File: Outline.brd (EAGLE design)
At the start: 53.8 x 53.8 mm, 51 parts, among them CN1 0675031020, IC1 ATXMEGA32A4U-AU, IC2 ST1480ACDR, J1 RJHSE5080, J2 J2, U1 NCP1117DTAG @ 3.3v, U2 NCP1117DTAG @ 12v

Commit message: 4.2.4
Final Version Submitted aka v1.0
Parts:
- moved C15 0.51 mm to (44.2, 19.8)
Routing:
- net +12V: track 85.4 -> 86.2 mm
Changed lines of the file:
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@@
 </element>
 <element name="C7" library="SparkFun" package="0603-CAP" value=".1uF" x="47.4321" y="40.4558125" smashed="yes">
-<attribute name="NAME" x="49.110178125" y="40.065784375" size="0.8128" layer="25"/>
+<attribute name="NAME" x="46.697178125" y="41.335784375" size="0.8128" layer="25"/>
 </element>
 <element name="DRV0" library="1dah" package="SOT89-5" value="PT4115" x="7.112" y="34.544">
@@
 </element>
 <element name="R8" library="nonolith" package="0805" value="300m Ohm" x="3.81" y="8.382" smashed="yes" rot="R180">
-<attribute name="NAME" x="5.842" y="7.493" size="0.8128" layer="25" font="vector" ratio="10"/>
+<attribute name="NAME" x="0.254" y="7.239" size="0.8128" layer="25" font="vector" ratio="10"/>
 </element>
 <element name="DRV2" library="1dah" package="SOT89-5" value="PT4115" x="12.446" y="12.446" rot="R180">
@@
 </element>
 <element name="R9" library="nonolith" package="0805" value="300 mOhm" x="12.192" y="8.382" smashed="yes" rot="R180">
-<attribute name="NAME" x="14.224" y="7.493" size="0.8128" layer="25" font="vector" ratio="10"/>
+<attribute name="NAME" x="8.636" y="7.239" size="0.8128" layer="25" font="vector" ratio="10"/>
 </element>
 <element name="J1" library="TechIsCool" package="RJHSE5080" value="RJHSE5080" x="19.304" y="-1.016" smashed="yes">
@@
 </element>
 <element name="R10" library="nonolith" package="0603" value="10k Ohm" x="50.8" y="40.38599375" smashed="yes">
-<attribute name="NAME" x="49.149" y="40.76700625" size="0.8128" layer="25" ratio="10" rot="R180"/>
+<attribute name="NAME" x="52.70499375" y="41.402" size="0.8128" layer="25" ratio="10" rot="R270"/>
 </element>
 <element name="R11" library="nonolith" package="0603" value="1k Ohm" x="50.79999375" y="42.545" smashed="yes">
-<attribute name="NAME" x="46.98999375" y="42.164" size="0.8128" layer="25" ratio="10"/>
+<attribute name="NAME" x="49.78399375" y="43.434" size="0.8128" layer="25" ratio="10"/>
 </element>
 <element name="R12" library="nonolith" package="0603" value="10k Ohm" x="46.30728125" y="50.950375" smashed="yes" rot="R90">
@@
 </element>
 <element name="R15" library="nonolith" package="0603" value="10k" x="40.1828" y="32.766" smashed="yes" rot="R270">
-<attribute name="NAME" x="40.5638" y="34.417" size="0.762" layer="25" ratio="10" rot="R90"/>
+<attribute name="NAME" x="40.259" y="35.2298" size="0.762" layer="25" ratio="10" rot="R180"/>
 </element>
 <element name="C9" library="SparkFun" package="0603-CAP" value=".1uF" x="2.286" y="43.942" smashed="yes" rot="R270">
@@
 <attribute name="NAME" x="51.816" y="10.668" size="0.8128" layer="25" rot="R180"/>
 </element>
-<element name="C15" library="SparkFun" package="0603-CAP" value=".1uF" x="44.196" y="19.304" smashed="yes" rot="R180">
-<attribute name="NAME" x="42.545" y="19.685" size="0.8128" layer="25" rot="R180"/>
+<element name="C15" library="SparkFun" package="0603-CAP" value=".1uF" x="44.196" y="19.812" smashed="yes" rot="R180">
+<attribute name="NAME" x="42.545" y="20.193" size="0.8128" layer="25" rot="R180"/>
 </element>
 <element name="U$1" library="TechIsCool" package="DMG1012T" value="DMG1012T" x="49.784" y="7.366" smashed="yes" rot="R180"/>
@@
 </element>
 <element name="U$3" library="TechIsCool" package="10W_LED" value="10W_RGB_LED" x="27.0256" y="26.5684" smashed="yes">
-<attribute name="NAME" x="36.3336" y="32.3494" size="1.27" layer="25" font="vector"/>
 <attribute name="VALUE" x="20.5856" y="26.9534" size="1.27" layer="27" font="vector"/>
 </element>
@@
 <contactref element="CN1" pad="GND@4"/>
 <contactref element="R15" pad="2"/>
-<via x="15.113" y="32.004" extent="1-16" drill="0.6" diameter="0.8128"/>
+<via x="13.716" y="32.004" extent="1-16" drill="0.6" diameter="0.8128"/>
 <via x="12.446" y="49.022" extent="1-16" drill="0.6" diameter="0.8128"/>
 <via x="5.461" y="12.192" extent="1-16" drill="0.6" diameter="0.8128"/>
@@
 <wire x1="48.2574" y1="38.0974" x2="46.3148" y2="38.0974" width="0.4064" layer="1"/>
 <wire x1="38.354" y1="33.186" x2="38.354" y2="33.274" width="0.4064" layer="1"/>
-<via x="40.513" y="35.433" extent="1-16" drill="0.6" diameter="0.8128"/>
+<via x="41.021" y="35.433" extent="1-16" drill="0.6" diameter="0.8128"/>
 <wire x1="19.47084375" y1="41.695840625" x2="19.812" y2="42.036996875" width="0.4064" layer="1"/>
 <wire x1="19.47084375" y1="41.695840625" x2="19.939003125" y2="42.164" width="0.4064" layer="16"/>
@@
 <wire x1="42.9182" y1="14.7946" x2="44.7816" y2="16.658" width="0.8128" layer="1"/>
 <wire x1="44.7816" y1="16.658" x2="45.046" y2="16.9224" width="0.8128" layer="1"/>
-<wire x1="45.046" y1="16.9224" x2="45.046" y2="19.304" width="0.8128" layer="1"/>
-<wire x1="45.046" y1="19.304" x2="47.2968" y2="21.5548" width="0.8128" layer="1"/>
-<wire x1="47.2968" y1="21.5548" x2="48.0412" y2="21.5548" width="0.8128" layer="1"/>
+<wire x1="45.046" y1="16.9224" x2="45.046" y2="19.812" width="0.8128" layer="1"/>
+<wire x1="47.2968" y1="21.5548" x2="47.752" y2="21.5548" width="0.8128" layer="1"/>
+<wire x1="47.752" y1="21.5548" x2="48.0412" y2="21.5548" width="0.8128" layer="1"/>
 <wire x1="41.148" y1="12.7" x2="42.125" y2="13.677" width="0.8128" layer="1"/>
 <wire x1="42.125" y1="13.677" x2="42.926" y2="13.677" width="0.8128" layer="1"/>
@@
 <wire x1="11.684" y1="17.78" x2="11.684" y2="34.036" width="0.8128" layer="16"/>
 <wire x1="11.684" y1="34.036" x2="11.176" y2="34.544" width="0.8128" layer="16"/>
+<wire x1="45.046" y1="19.812" x2="46.0092" y2="19.812" width="0.8128" layer="1"/>
+<wire x1="46.0092" y1="19.812" x2="47.752" y2="21.5548" width="0.8128" layer="1"/>
 </signal>
 <signal name="N$2">

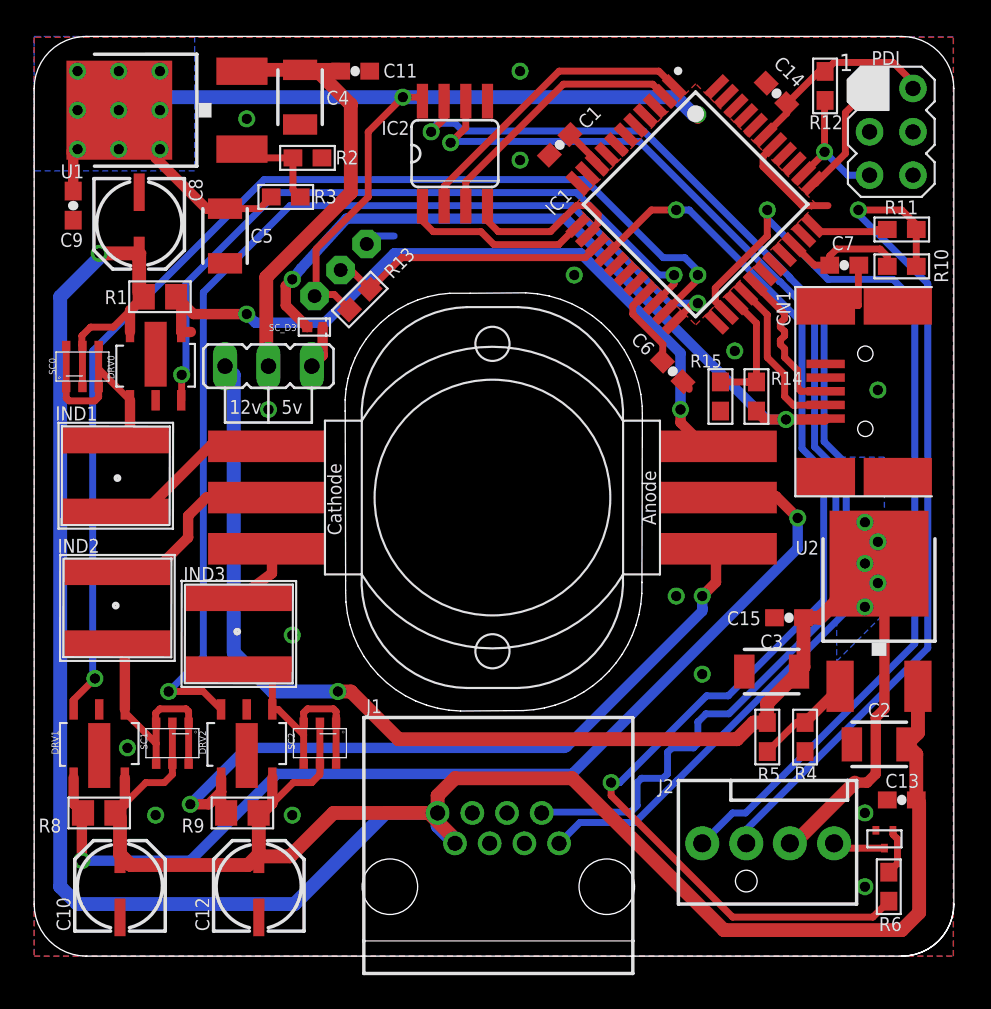
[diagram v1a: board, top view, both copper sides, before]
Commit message: 4.3
Changed LDO resistor values to stop overheating. Added 68pf cap between
reset and ground to make AVR Dragon talk with device.
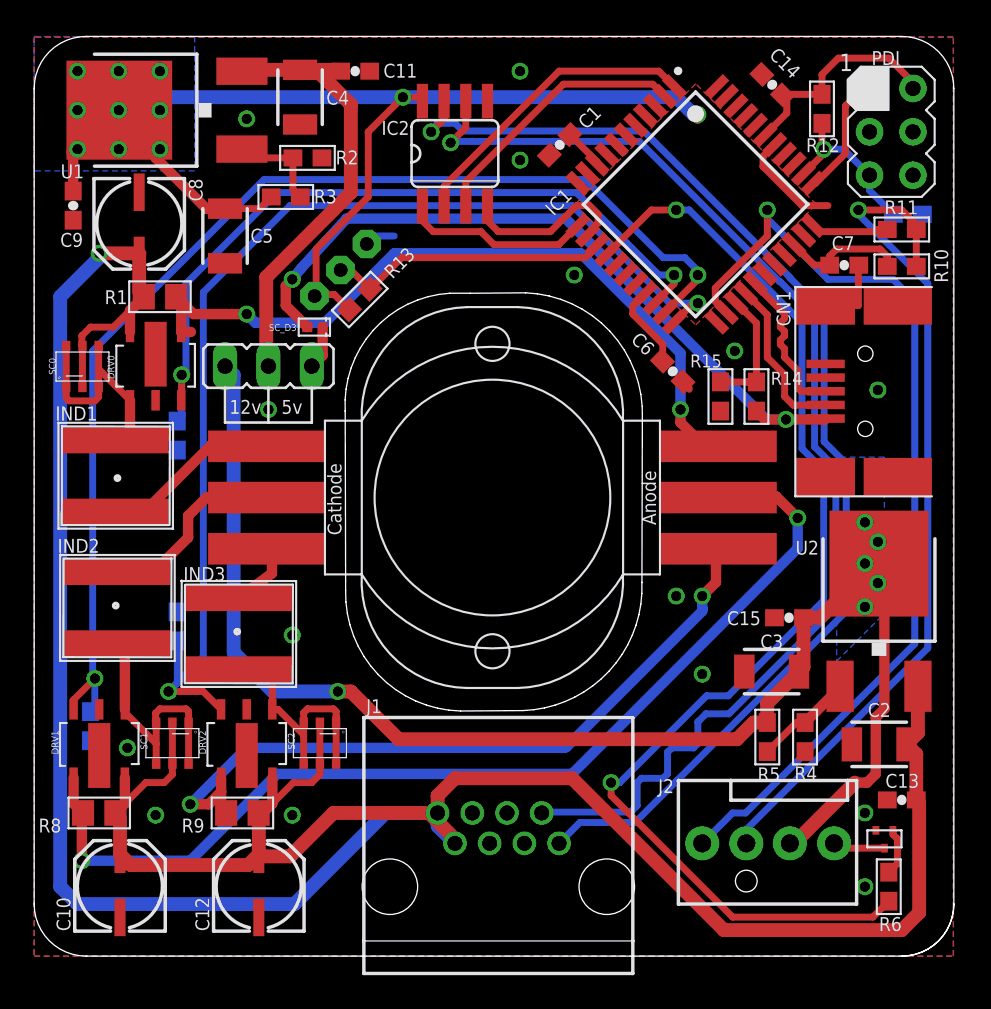
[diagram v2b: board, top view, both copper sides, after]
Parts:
- added C16: 68pF, SparkFun:0603-CAP
- added R16, R17, R7: 47k Ohm, nonolith:0603
- R2: value 15 Ohms -> 412 Ohms
- R3: value 9.09 Ohms -> 255 Ohms
- R4: value 102 Ohms -> 2k Ohms
- R5: value 11.8 Ohms -> 237 Ohms
- moved R12 1.36 mm to (46.1, 49.6)
- moved C14 0.57 mm to (43.2, 51.0)
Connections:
- net GND: now also C16.2, R16.1, R17.1, R7.1
- net N$22: now also C16.1
- net PWM0: now also R7.2
- net PWM1: now also R16.2
- net PWM2: now also R17.2
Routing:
- net PWM2: track 63.0 -> 66.1 mm
- net PWM0: track 41.8 -> 44.6 mm
- net PWM1: track 66.6 -> 68.7 mm
- net N$22: track 8.02 -> 9.87 mm
- net +3V3: track 92.0 -> 93.5 mm
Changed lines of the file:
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@@
 <attribute name="NAME" x="30.406821875" y="43.2998875" size="0.8128" layer="21" ratio="5" rot="R45"/>
 </element>
-<element name="R2" library="nonolith" package="0603" value="15 Ohms" x="16.002" y="46.736" smashed="yes" rot="R180">
+<element name="R2" library="nonolith" package="0603" value="412 Ohms" x="16.002" y="46.736" smashed="yes" rot="R180">
 <attribute name="NAME" x="17.653" y="46.355" size="0.8128" layer="25" ratio="10"/>
 </element>
-<element name="R3" library="nonolith" package="0603" value="9.09 Ohms" x="14.732" y="44.45" smashed="yes" rot="R180">
+<element name="R3" library="nonolith" package="0603" value="255 Ohms" x="14.732" y="44.45" smashed="yes" rot="R180">
 <attribute name="NAME" x="16.383" y="44.069" size="0.8128" layer="25" ratio="10"/>
 </element>
-<element name="R4" library="nonolith" package="0603" value="102 Ohms" x="45.1358" y="12.827" smashed="yes" rot="R90">
+<element name="R4" library="nonolith" package="0603" value="2k Ohms" x="45.1358" y="12.827" smashed="yes" rot="R90">
 <attribute name="NAME" x="45.847" y="11.0998" size="0.8128" layer="25" ratio="10" rot="R180"/>
 </element>
-<element name="R5" library="nonolith" package="0603" value="11.8 Ohms" x="42.926" y="12.827" smashed="yes" rot="R90">
+<element name="R5" library="nonolith" package="0603" value="237 Ohms" x="42.926" y="12.827" smashed="yes" rot="R90">
 <attribute name="NAME" x="43.688" y="11.049" size="0.8128" layer="25" ratio="10" rot="R180"/>
 </element>
@@
 <attribute name="NAME" x="49.78399375" y="43.434" size="0.8128" layer="25" ratio="10"/>
 </element>
-<element name="R12" library="nonolith" package="0603" value="10k Ohm" x="46.30728125" y="50.950375" smashed="yes" rot="R90">
-<attribute name="NAME" x="47.347625" y="49.22828125" size="0.8128" layer="25" ratio="10" rot="R180"/>
-</element>
-<element name="C14" library="SparkFun" package="0603-CAP" value=".1uF" x="43.467365625" y="50.51263125" smashed="yes" rot="R135">
-<attribute name="NAME" x="45.208165625" y="51.377196875" size="0.8128" layer="25" rot="R135"/>
+<element name="R12" library="nonolith" package="0603" value="10k Ohm" x="46.127671875" y="49.605978125" smashed="yes" rot="R90">
+<attribute name="NAME" x="47.16801875" y="47.883884375" size="0.8128" layer="25" ratio="10" rot="R180"/>
+</element>
+<element name="C14" library="SparkFun" package="0603-CAP" value=".1uF" x="43.213365625" y="51.02063125" smashed="yes" rot="R135">
+<attribute name="NAME" x="44.954165625" y="51.885196875" size="0.8128" layer="25" rot="R135"/>
 </element>
 <element name="U$2" library="TechIsCool" package="TOP-92-INLINE" value="DS18B20" x="17.9442" y="40.1692" smashed="yes" rot="MR315">
@@
 <attribute name="VALUE" x="20.5856" y="26.9534" size="1.27" layer="27" font="vector"/>
 </element>
+<element name="C16" library="SparkFun" package="0603-CAP" value="68pF" x="51.159209375" y="43.434" rot="MR180"/>
+<element name="R7" library="nonolith" package="0603" value="47k Ohm" x="8.382" y="30.48" rot="MR90"/>
+<element name="R16" library="nonolith" package="0603" value="47k Ohm" x="3.302" y="13.462" rot="MR90"/>
+<element name="R17" library="nonolith" package="0603" value="47k Ohm" x="8.382" y="19.304" rot="MR270"/>
 </elements>
 <signals>
@@
 <via x="38.862" y="49.276" extent="1-16" drill="0.6" diameter="0.8128"/>
 <wire x1="38.862" y1="49.276" x2="38.862" y2="49.022" width="0.6096" layer="1"/>
-<wire x1="46.30728125" y1="51.800375" x2="46.83090625" y2="52.324" width="0.4064" layer="1"/>
-<wire x1="46.83090625" y1="52.324" x2="50.292" y2="52.324" width="0.4064" layer="1"/>
-<wire x1="50.292" y1="52.324" x2="51.454765625" y2="51.161234375" width="0.4064" layer="1"/>
+<wire x1="50.038" y1="52.578" x2="51.454765625" y2="51.161234375" width="0.4064" layer="1"/>
 <wire x1="51.454765625" y1="51.161234375" x2="51.454765625" y2="50.804134375" width="0.4064" layer="1"/>
 <contactref element="C14" pad="1"/>
@@
 <wire x1="31.36915625" y1="48.10085" x2="32.964965625" y2="46.505040625" width="0.4064" layer="1"/>
 <wire x1="32.964965625" y1="46.505040625" x2="32.964965625" y2="46.383984375" width="0.4064" layer="1"/>
-<wire x1="44.06840625" y1="49.9115875" x2="44.06840625" y2="49.355696875" width="0.4064" layer="1"/>
 <wire x1="44.06840625" y1="49.355696875" x2="42.79375" y2="48.081040625" width="0.4064" layer="1"/>
-<wire x1="44.06840625" y1="49.9115875" x2="45.95719375" y2="51.800375" width="0.4064" layer="1"/>
-<wire x1="45.95719375" y1="51.800375" x2="46.30728125" y2="51.800375" width="0.4064" layer="1"/>
 <contactref element="U$2" pad="3"/>
 <contactref element="R13" pad="2"/>
@@
 <wire x1="37.592" y1="50.292" x2="38.608" y2="49.276" width="0.8128" layer="16"/>
 <wire x1="38.608" y1="49.276" x2="38.862" y2="49.276" width="0.8128" layer="16"/>
+<wire x1="44.06840625" y1="49.355696875" x2="44.06840625" y2="50.4195875" width="0.4064" layer="1"/>
+<wire x1="44.06840625" y1="50.4195875" x2="43.81440625" y2="50.4195875" width="0.4064" layer="1"/>
+<wire x1="44.06840625" y1="50.4195875" x2="44.104796875" y2="50.455978125" width="0.4064" layer="1"/>
+<wire x1="44.104796875" y1="50.455978125" x2="46.127671875" y2="50.455978125" width="0.4064" layer="1"/>
+<wire x1="46.127671875" y1="50.455978125" x2="46.127671875" y2="51.620765625" width="0.4064" layer="1"/>
+<wire x1="50.038" y1="52.578" x2="47.08490625" y2="52.578" width="0.4064" layer="1"/>
+<wire x1="47.08490625" y1="52.578" x2="46.127671875" y2="51.620765625" width="0.4064" layer="1"/>
 </signal>
 <signal name="N$1">
@@
 <contactref element="J1" pad="P$4"/>
 <contactref element="J1" pad="P$3"/>
+<contactref element="C16" pad="2"/>
+<contactref element="R17" pad="1"/>
+<contactref element="R16" pad="1"/>
+<contactref element="R7" pad="1"/>
 </signal>
 <signal name="+12V">
@@
 <wire x1="36.576" y1="39.878" x2="37.465" y2="39.878" width="0.4064" layer="16"/>
 <wire x1="37.465" y1="39.358178125" x2="37.465" y2="39.878" width="0.4064" layer="1"/>
+<contactref element="R7" pad="2"/>
+<wire x1="8.382" y1="31.33" x2="8.636" y2="31.584" width="0.4064" layer="16" curve="90"/>
+<wire x1="8.636" y1="31.584" x2="8.636" y2="34.036" width="0.4064" layer="16"/>
 </signal>
 <signal name="N$9">
@@
 <wire x1="38.099809375" y1="40.894" x2="38.862" y2="40.131809375" width="0.4064" layer="16"/>
 <wire x1="38.862" y1="40.131809375" x2="38.862" y2="39.878" width="0.4064" layer="16"/>
+<contactref element="R16" pad="2"/>
+<wire x1="3.302" y1="14.312" x2="3.556" y2="14.566" width="0.4064" layer="16"/>
+<wire x1="3.556" y1="14.566" x2="3.556" y2="16.256" width="0.4064" layer="16"/>
 </signal>
 <signal name="PWM2">
@@
 <wire x1="38.596565625" y1="38.227" x2="38.862" y2="38.227" width="0.4064" layer="1"/>
 <wire x1="31.496" y1="43.942" x2="37.211" y2="38.227" width="0.4064" layer="16"/>
+<contactref element="R17" pad="2"/>
+<wire x1="8.382" y1="18.454" x2="8.382" y2="16.002" width="0.4064" layer="16"/>
+<wire x1="8.382" y1="16.002" x2="7.874" y2="15.494" width="0.4064" layer="16"/>
 </signal>
 <signal name="RS485_N">
@@
 <contactref element="IC1" pad="35"/>
 <contactref element="R12" pad="1"/>
-<via x="46.2788" y="47.0916" extent="1-16" drill="0.6" diameter="0.8128"/>
-<wire x1="45.056490625" y1="45.8183" x2="46.2788" y2="47.040609375" width="0.4064" layer="1"/>
-<wire x1="46.2788" y1="47.040609375" x2="46.2788" y2="47.0916" width="0.4064" layer="1"/>
-<wire x1="46.2788" y1="50.100375" x2="46.30728125" y2="50.100375" width="0.4064" layer="1"/>
-<wire x1="46.2788" y1="47.0916" x2="47.646265625" y2="45.724134375" width="0.4064" layer="16"/>
-<wire x1="47.646265625" y1="45.724134375" x2="48.914765625" y2="45.724134375" width="0.4064" layer="16"/>
-<wire x1="46.2788" y1="50.100375" x2="46.2788" y2="47.0916" width="0.4064" layer="1"/>
+<contactref element="C16" pad="1"/>
+<wire x1="48.914765625" y1="45.724134375" x2="48.914765625" y2="44.82844375" width="0.4064" layer="16"/>
+<wire x1="48.914765625" y1="44.82844375" x2="50.309209375" y2="43.434" width="0.4064" layer="16"/>
+<wire x1="45.056490625" y1="45.8183" x2="46.228" y2="46.989809375" width="0.4064" layer="1"/>
+<wire x1="45.974190625" y1="48.602496875" x2="46.127671875" y2="48.755978125" width="0.4064" layer="1"/>
+<wire x1="48.914765625" y1="45.724134375" x2="47.3949" y2="47.244" width="0.4064" layer="16"/>
+<via x="46.228" y="47.244" extent="1-16" drill="0.6" diameter="0.8128"/>
+<wire x1="46.127671875" y1="47.397671875" x2="46.127671875" y2="47.498" width="0.4064" layer="1"/>
+<wire x1="46.127671875" y1="47.498" x2="46.127671875" y2="48.755978125" width="0.4064" layer="1"/>
+<wire x1="46.228" y1="46.989809375" x2="46.228" y2="47.244" width="0.4064" layer="1"/>
+<wire x1="46.228" y1="47.244" x2="46.127671875" y2="47.344328125" width="0.4064" layer="1"/>
+<wire x1="46.127671875" y1="47.344328125" x2="46.127671875" y2="47.397671875" width="0.4064" layer="1"/>
+<wire x1="46.228" y1="47.244" x2="47.3949" y2="47.244" width="0.4064" layer="16"/>
 </signal>
 <signal name="RX">
@@
 <wire x1="45.622178125" y1="45.2526125" x2="45.7606125" y2="45.2526125" width="0.4064" layer="1"/>
 <wire x1="45.7606125" y1="45.2526125" x2="47.498" y2="46.99" width="0.4064" layer="1"/>
-<wire x1="47.498" y1="46.99" x2="47.498" y2="49.38736875" width="0.4064" layer="1"/>
-<wire x1="47.498" y1="49.38736875" x2="48.914765625" y2="50.804134375" width="0.4064" layer="1"/>
+<wire x1="47.498" y1="46.99" x2="47.498" y2="49.784" width="0.4064" layer="1"/>
+<wire x1="47.498" y1="49.784" x2="48.518134375" y2="50.804134375" width="0.4064" layer="1"/>
+<wire x1="48.518134375" y1="50.804134375" x2="48.914765625" y2="50.804134375" width="0.4064" layer="1"/>
 </signal>
 <signal name="RED_A">
